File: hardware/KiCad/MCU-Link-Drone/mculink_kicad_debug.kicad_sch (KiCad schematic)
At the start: 43 parts, among them J1 Pixhawk Debug Full, J2 Pixhawk_Debug_Mini, J6 Conn_02x05_Odd_Even, J8 DCD-LZ_Debug, SW2 KMR221GLFS, U3 74LVC2T45DC, U4 SN74LVC1T45GW, U5 SN74LVC1T45GW, U6 MCP6001-OT, U7 SN74LVC1T45GW

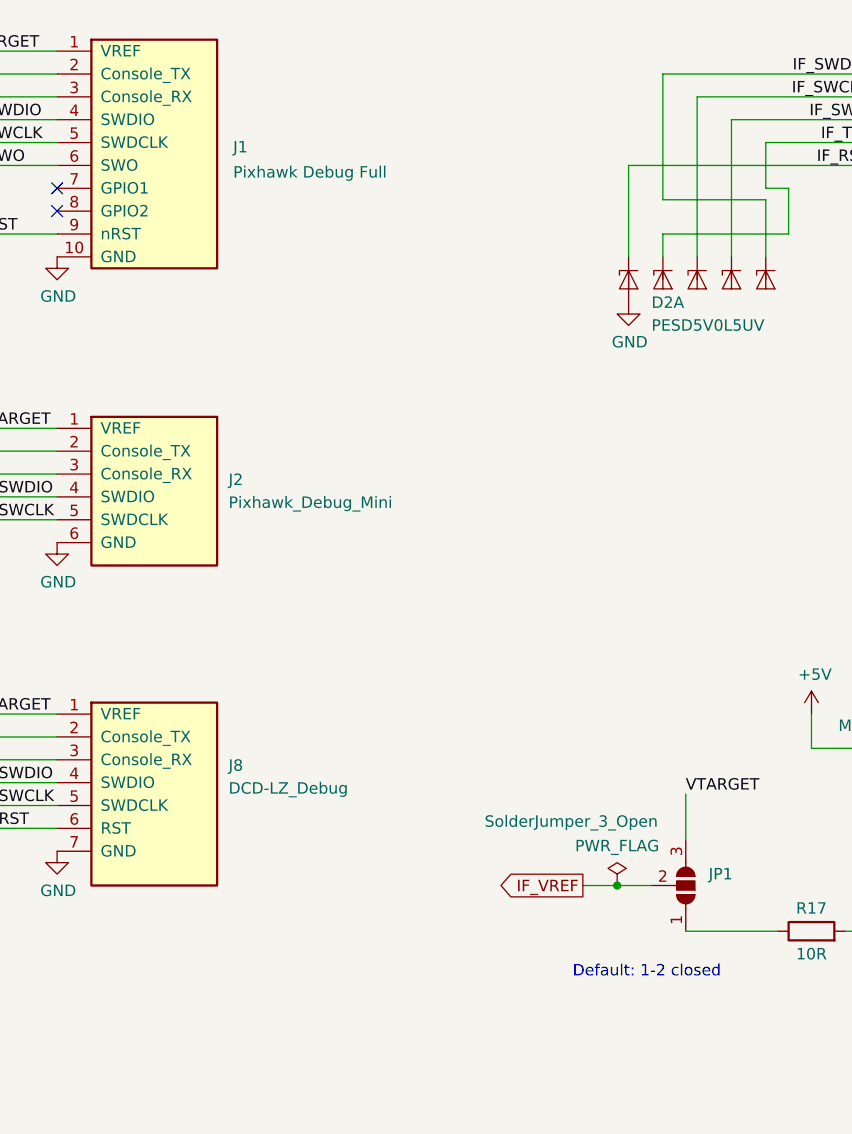
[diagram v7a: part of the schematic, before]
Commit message: production files for V0.1
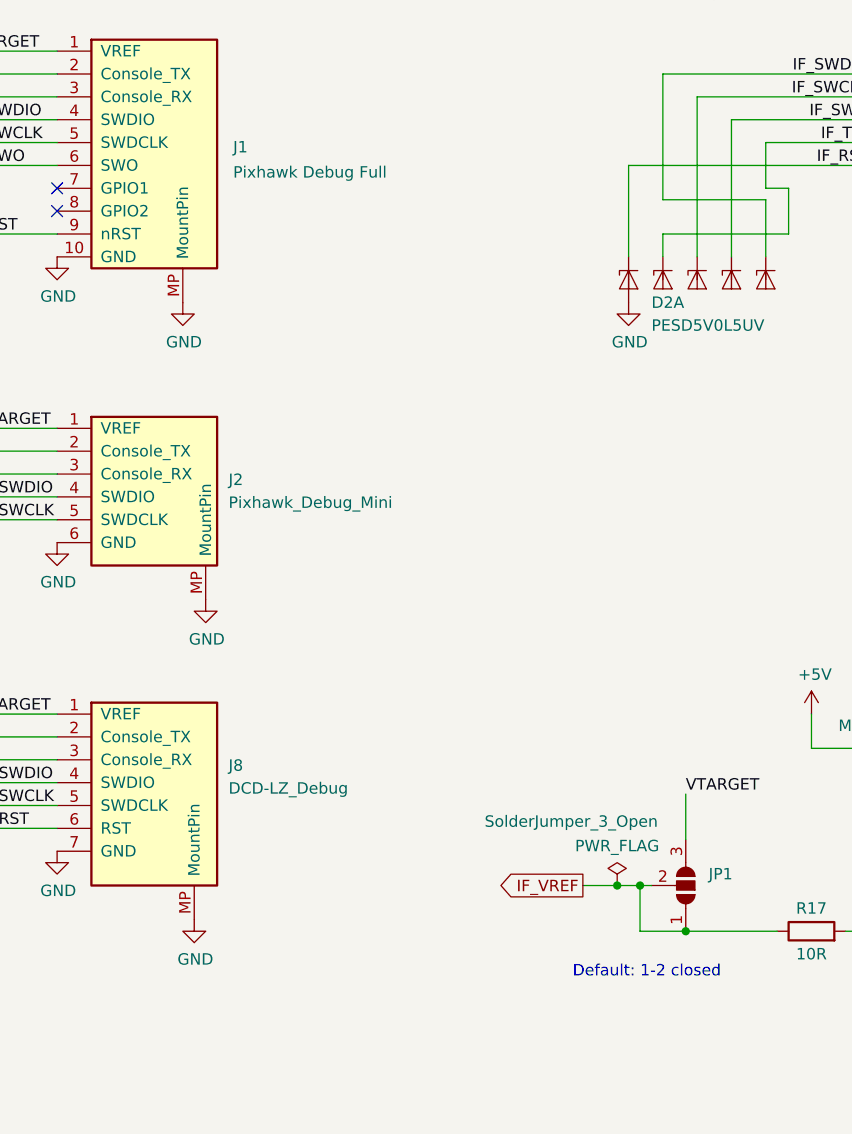
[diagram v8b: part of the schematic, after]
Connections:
- net GND: now also J1.MP (MountPin), J2.MP (MountPin), J8.MP (MountPin)
- net IF_VREF: now also JP1.1 (A), R17.1
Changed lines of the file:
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@@
 	)
 	(junction
+		(at 207.01 139.7)
+		(diameter 0)
+		(color 0 0 0 0)
+	)
+	(junction
 		(at 242.57 48.26)
 		(diameter 0)
@@
 	)
 	(junction
+		(at 201.93 134.62)
+		(diameter 0)
+		(color 0 0 0 0)
+	)
+	(junction
 		(at 49.53 143.51)
 		(diameter 0)
@@
 	(wire
 		(pts
+			(xy 201.93 134.62) (xy 203.2 134.62)
+		)
+		(stroke
+			(width 0)
+			(type default)
+		)
+	)
+	(wire
+		(pts
 			(xy 242.57 48.26) (xy 242.57 46.99)
 		)
@@
 	(wire
 		(pts
+			(xy 207.01 139.7) (xy 201.93 139.7)
+		)
+		(stroke
+			(width 0)
+			(type default)
+		)
+	)
+	(wire
+		(pts
 			(xy 39.37 87.63) (xy 39.37 86.36)
 		)
@@
 	(wire
 		(pts
-			(xy 199.39 134.62) (xy 203.2 134.62)
+			(xy 199.39 134.62) (xy 201.93 134.62)
 		)
 		(stroke
@@
 	(wire
 		(pts
+			(xy 201.93 139.7) (xy 201.93 134.62)
+		)
+		(stroke
+			(width 0)
+			(type default)
+		)
+	)
+	(wire
+		(pts
 			(xy 128.27 123.19) (xy 137.16 123.19)
 		)
@@
 		(pin "10"
 		)
+		(pin "MP"
+		)
 		(instances
 			(project "mculink_drone_kicad"
@@
 	)
 	(symbol
+		(lib_id "power:GND")
+		(at 153.67 102.87 0)
+		(unit 1)
+		(exclude_from_sim no)
+		(in_bom yes)
+		(on_board yes)
+		(dnp no)
+		(property "Reference" "#PWR090"
+			(at 153.67 109.22 0)
+			(effects
+				(font
+					(size 1.27 1.27)
+				)
+				(hide yes)
+			)
+		)
+		(property "Value" "GND"
+			(at 153.797 107.2642 0)
+			(effects
+				(font
+					(size 1.27 1.27)
+				)
+			)
+		)
+		(property "Footprint" ""
+			(at 153.67 102.87 0)
+			(effects
+				(font
+					(size 1.27 1.27)
+				)
+				(hide yes)
+			)
+		)
+		(property "Datasheet" ""
+			(at 153.67 102.87 0)
+			(effects
+				(font
+					(size 1.27 1.27)
+				)
+				(hide yes)
+			)
+		)
+		(property "Description" "Power symbol creates a global label with name \"GND\" , ground"
+			(at 153.67 102.87 0)
+			(effects
+				(font
+					(size 1.27 1.27)
+				)
+				(hide yes)
+			)
+		)
+		(pin "1"
+		)
+		(instances
+			(project "mculink_drone_kicad"
+				(path "/5d025764-753a-4b80-8d3d-c9a8a22c9527/00000000-0000-0000-0000-0000603cff19"
+					(reference "#PWR090")
+					(unit 1)
+				)
+			)
+		)
+	)
+	(symbol
 		(lib_id "power:PWR_FLAG")
 		(at 240.03 125.73 90)
@@
 		(pin "7"
 		)
+		(pin "MP"
+		)
 		(instances
 			(project "mculink_drone_kicad"
@@
 	(symbol
 		(lib_id "power:GND")
+		(at 152.4 138.43 0)
+		(unit 1)
+		(exclude_from_sim no)
+		(in_bom yes)
+		(on_board yes)
+		(dnp no)
+		(property "Reference" "#PWR096"
+			(at 152.4 144.78 0)
+			(effects
+				(font
+					(size 1.27 1.27)
+				)
+				(hide yes)
+			)
+		)
+		(property "Value" "GND"
+			(at 152.527 142.8242 0)
+			(effects
+				(font
+					(size 1.27 1.27)
+				)
+			)
+		)
+		(property "Footprint" ""
+			(at 152.4 138.43 0)
+			(effects
+				(font
+					(size 1.27 1.27)
+				)
+				(hide yes)
+			)
+		)
+		(property "Datasheet" ""
+			(at 152.4 138.43 0)
+			(effects
+				(font
+					(size 1.27 1.27)
+				)
+				(hide yes)
+			)
+		)
+		(property "Description" "Power symbol creates a global label with name \"GND\" , ground"
+			(at 152.4 138.43 0)
+			(effects
+				(font
+					(size 1.27 1.27)
+				)
+				(hide yes)
+			)
+		)
+		(pin "1"
+		)
+		(instances
+			(project "mculink_drone_kicad"
+				(path "/5d025764-753a-4b80-8d3d-c9a8a22c9527/00000000-0000-0000-0000-0000603cff19"
+					(reference "#PWR096")
+					(unit 1)
+				)
+			)
+		)
+	)
+	(symbol
+		(lib_id "power:GND")
 		(at 254 100.33 0)
 		(unit 1)
@@
 		(pin "1"
 		)
+		(pin "MP"
+		)
 		(instances
 			(project "mculink_drone_kicad"
@@
 					(unit 1)
 				)
+			)
+		)
+	)
+	(symbol
+		(lib_id "power:GND")
+		(at 151.13 69.85 0)
+		(unit 1)
+		(exclude_from_sim no)
+		(in_bom yes)
+		(on_board yes)
+		(dnp no)
+		(property "Reference" "#PWR089"
+			(at 151.13 76.2 0)
+			(effects
+				(font
+					(size 1.27 1.27)
+				)
+				(hide yes)
+			)
+		)
+		(property "Value" "GND"
+			(at 151.257 74.2442 0)
+			(effects
+				(font
+					(size 1.27 1.27)
+				)
+			)
+		)
+		(property "Footprint" ""
+			(at 151.13 69.85 0)
+			(effects
+				(font
+					(size 1.27 1.27)
+				)
+				(hide yes)
+			)
+		)
+		(property "Datasheet" ""
+			(at 151.13 69.85 0)
+			(effects
+				(font
+					(size 1.27 1.27)
+				)
+				(hide yes)
+			)
+		)
+		(property "Description" "Power symbol creates a global label with name \"GND\" , ground"
+			(at 151.13 69.85 0)
+			(effects
+				(font
+					(size 1.27 1.27)
+				)
+				(hide yes)
+			)
+		)
+		(pin "1"
+		)
+		(instances
+			(project "mculink_drone_kicad"
+				(path "/5d025764-753a-4b80-8d3d-c9a8a22c9527/00000000-0000-0000-0000-0000603cff19"
+					(reference "#PWR089")
+					(unit 1)
+				)
